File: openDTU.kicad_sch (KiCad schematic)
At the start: 9 parts, among them U1 ESP32NodeMCU, U2 NRF24L01+PA+LNA_Breakout

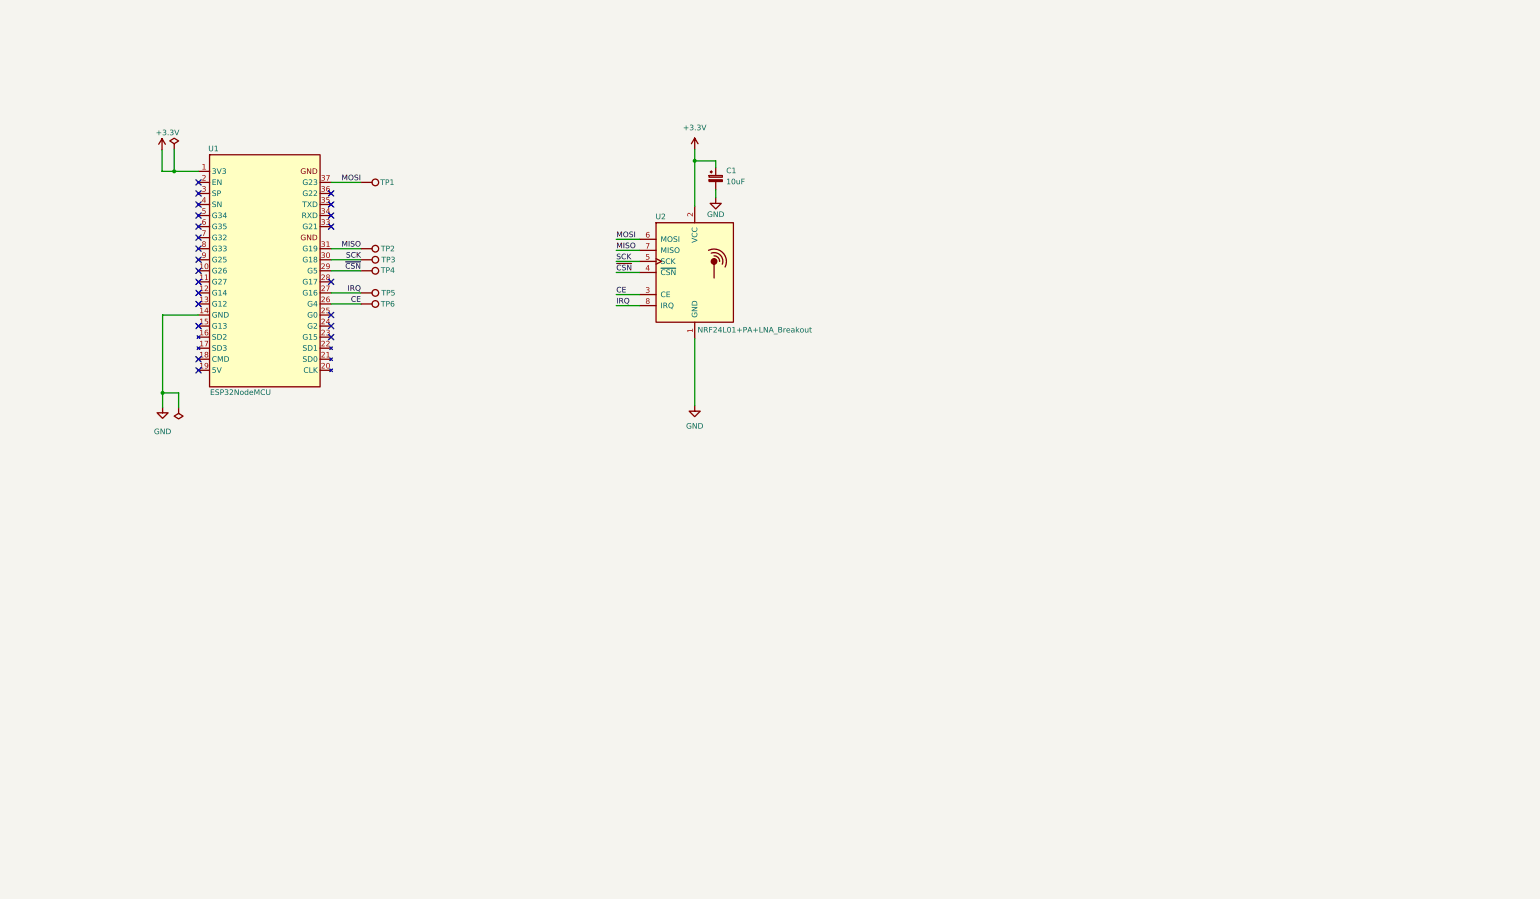
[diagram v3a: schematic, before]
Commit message: adding first SMT parts to schematic and PCB, like MCU and nRF24L01+
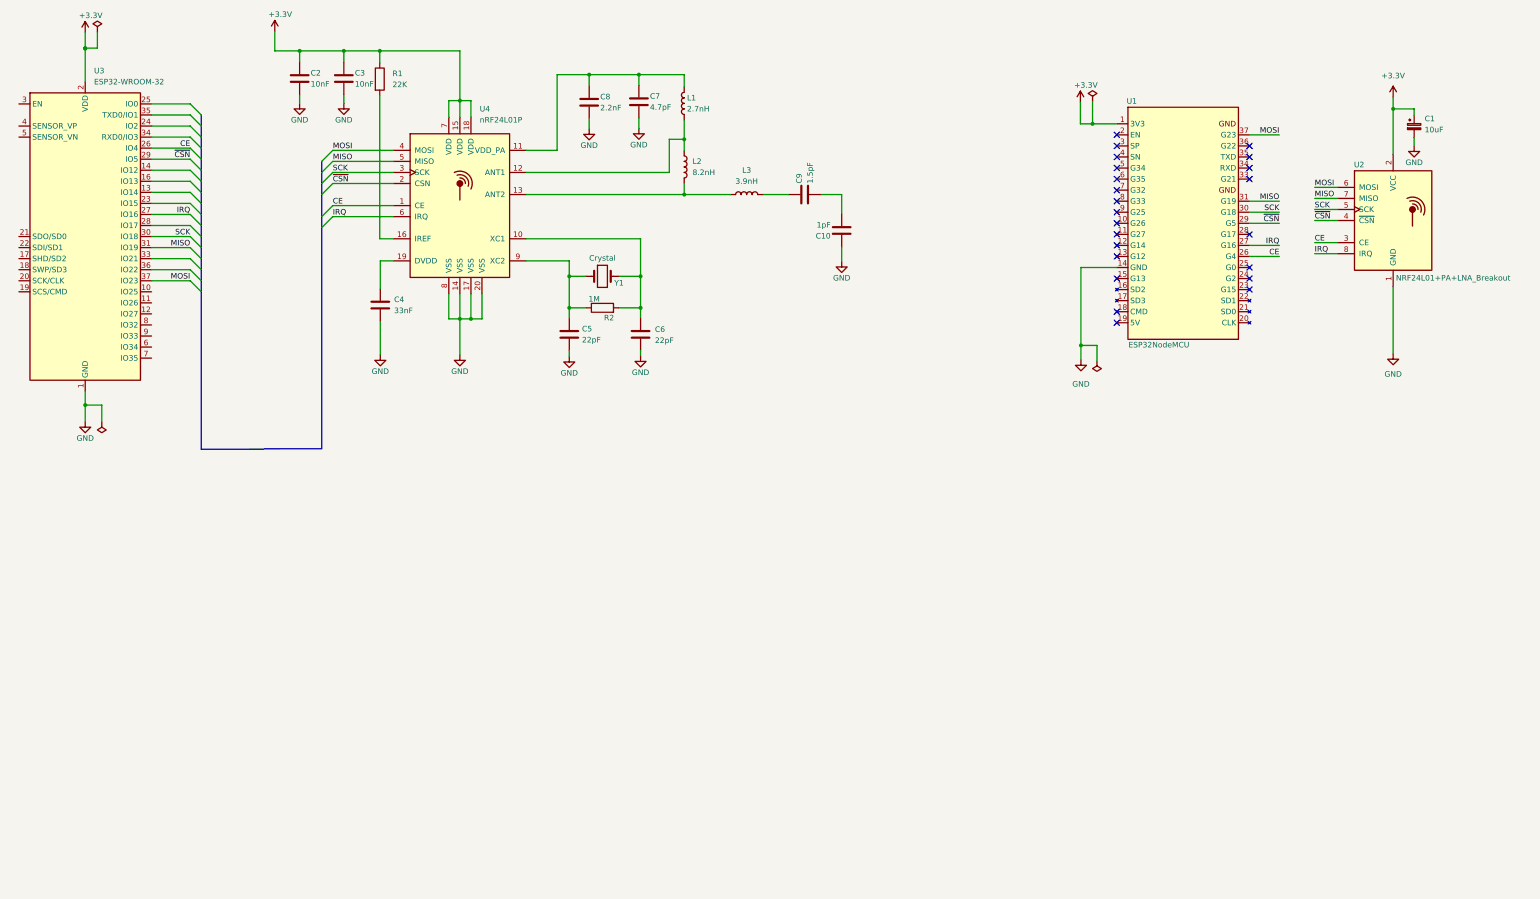
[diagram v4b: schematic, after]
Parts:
- removed TP1, TP2, TP3, TP4, TP5, TP6: TestPoint, TestPoint:TestPoint_THTPad_D1.5mm_Drill0.7mm, symbol Connector:TestPoint
- added C10: 1pF, Capacitor_SMD:C_0603_1608Metric_Pad1.08x0.95mm_HandSolder, symbol Device:C
- added C2, C3: 10nF, Capacitor_SMD:C_0603_1608Metric_Pad1.08x0.95mm_HandSolder, symbol Device:C
- added C4: 33nF, Capacitor_SMD:C_0603_1608Metric_Pad1.08x0.95mm_HandSolder, symbol Device:C
- added C5, C6: 22pF, Capacitor_SMD:C_0603_1608Metric_Pad1.08x0.95mm_HandSolder, symbol Device:C
- added C7: 4.7pF, Capacitor_SMD:C_0603_1608Metric_Pad1.08x0.95mm_HandSolder, symbol Device:C
- added C8: 2.2nF, Capacitor_SMD:C_0603_1608Metric_Pad1.08x0.95mm_HandSolder, symbol Device:C
- added C9: 1.5pF, Capacitor_SMD:C_0603_1608Metric_Pad1.08x0.95mm_HandSolder, symbol Device:C
- added L1: 2.7nH, Inductor_SMD:L_0603_1608Metric_Pad1.05x0.95mm_HandSolder, symbol Device:L
- added L2: 8.2nH, Inductor_SMD:L_0603_1608Metric_Pad1.05x0.95mm_HandSolder, symbol Device:L
- added L3: 3.9nH, Inductor_SMD:L_0603_1608Metric_Pad1.05x0.95mm_HandSolder, symbol Device:L
- added R1: 22K, Resistor_SMD:R_0603_1608Metric_Pad0.98x0.95mm_HandSolder, symbol Device:R
- added R2: 1M, Resistor_SMD:R_0603_1608Metric_Pad0.98x0.95mm_HandSolder, symbol Device:R
- added U3: ESP32-WROOM-32, RF_Module:ESP32-WROOM-32, symbol RF_Module:ESP32-WROOM-32
- added U4: nRF24L01P, Package_DFN_QFN:QFN-20-1EP_4x4mm_P0.5mm_EP2.5x2.5mm, symbol RF:nRF24L01P
- added Y1: Crystal, Crystal:Crystal_SMD_3225-4Pin_3.2x2.5mm, symbol Device:Crystal
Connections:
- net +3.3V: now also C2.1, C3.1, R1.1, U4.15 (VDD), U4.18 (VDD), U4.7 (VDD)
- net CE: now also U3.26 (IO4), U4.1 (CE)
- net GND: now also C10.1, C2.2, C3.2, C4.2, C5.2, C6.2, C7.2, C8.2, U3.1 (GND), U3.15 (GND), U3.38 (GND), U3.39 (GND), U4.14 (VSS), U4.17 (VSS), U4.20 (VSS), U4.8 (VSS)
- net IRQ: now also U3.27 (IO16), U4.6 (IRQ)
- net MISO: now also U3.31 (IO19), U4.5 (MISO)
- net MOSI: now also U3.37 (IO23), U4.4 (MOSI)
- net SCK: now also U3.30 (IO18), U4.3 (SCK)
- net ~{CSN}: now also U3.29 (IO5), U4.2 (CSN)
- new net: C7.1, C8.1, L1.2, U4.11 (VDD_PA)
- new net: C5.1, R2.1, U4.9 (XC2), Y1.1
- new net: C6.1, R2.2, U4.10 (XC1), Y1.2
- new net: L2.2, L3.1, U4.13 (ANT2)
- new net: C9.1, L3.2
- new net: C4.1, U4.19 (DVDD)
- new net: L1.1, L2.1, U4.12 (ANT1)
- new net: R1.2, U4.16 (IREF)
- new net: C10.2, C9.2
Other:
- title: (none) -> openDTU
- moved on the sheet: C1, U1, U2

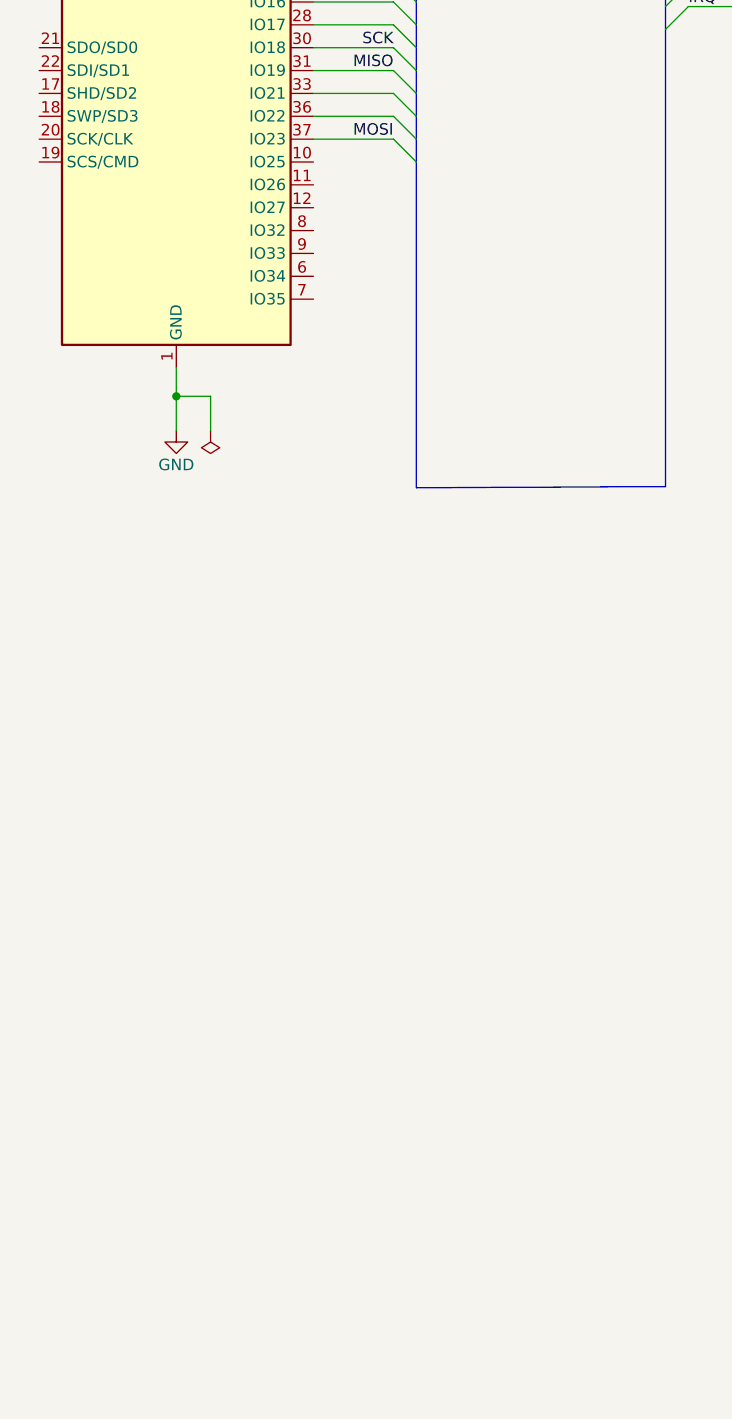
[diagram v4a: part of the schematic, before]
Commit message: adding USB-C connector for power supply
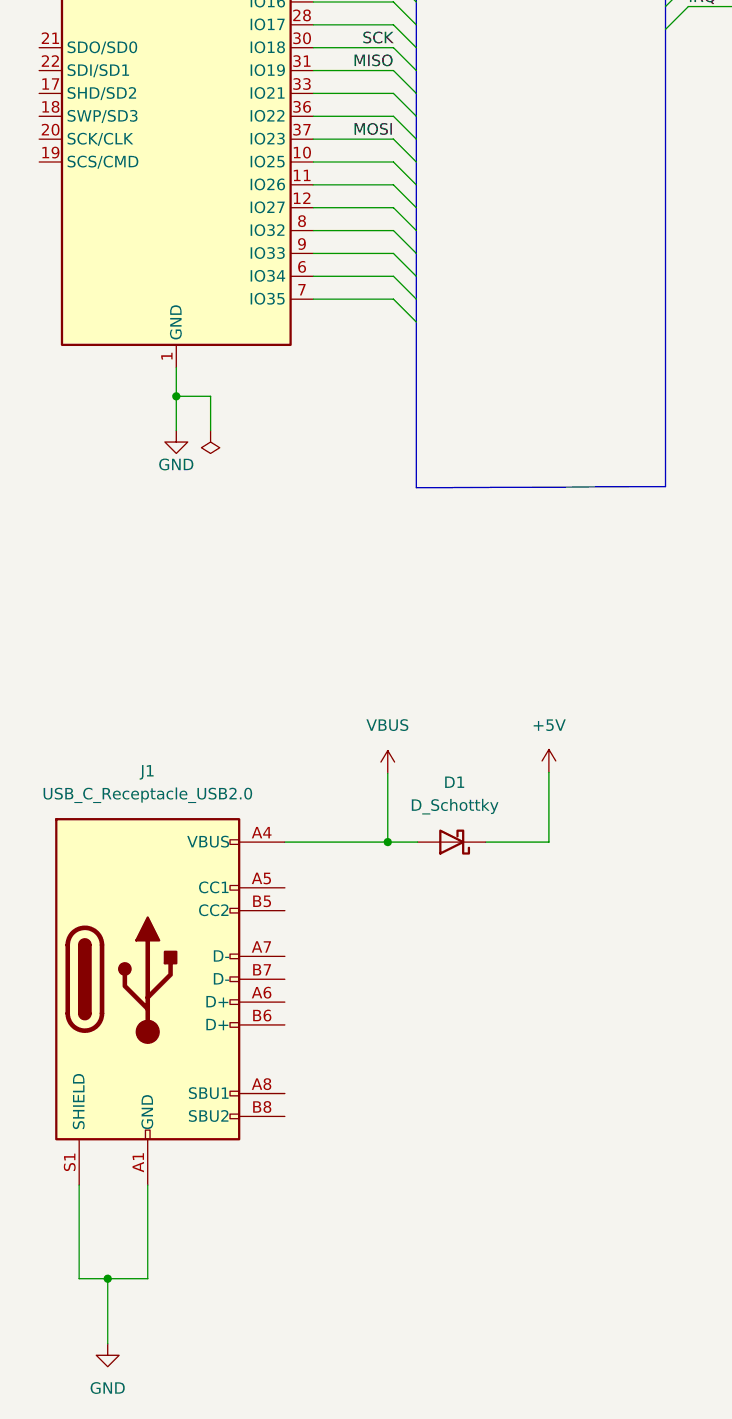
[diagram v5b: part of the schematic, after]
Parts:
- added D1: D_Schottky, Diode_SMD:D_1206_3216Metric, symbol Device:D_Schottky
- added J1: USB_C_Receptacle_USB2.0, symbol Connector:USB_C_Receptacle_USB2.0
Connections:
- net GND: now also J1.A1 (GND), J1.A12 (GND), J1.B1 (GND), J1.B12 (GND), J1.S1 (SHIELD)
- new net +5V: D1.1 (K)
- new net VBUS: D1.2 (A), J1.A4 (VBUS), J1.A9 (VBUS), J1.B4 (VBUS), J1.B9 (VBUS)
